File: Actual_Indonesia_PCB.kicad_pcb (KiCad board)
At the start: 2 copper layers, 157.7 x 133.2 mm, 88 parts, among them J1 USB_C_Receptacle_USB2.0_16P, J17 Screw_Terminal_01x02, J18 Screw_Terminal_01x02, J19 Screw_Terminal_01x02, J2 Conn_01x02_Pin, J20 Screw_Terminal_01x02, J21 Screw_Terminal_01x02, J22 Screw_Terminal_01x02, J23 Screw_Terminal_01x02, J24 Screw_Terminal_01x02, J25 Screw_Terminal_01x02, J26 Screw_Terminal_01x02, J27 Screw_Terminal_01x02, J28 Screw_Terminal_01x02, J29 Screw_Terminal_01x02, J30 Screw_Terminal_01x02, Q15 IRLZ44N, Q16 IRLZ44N, Q17 IRLZ44N, Q18 IRLZ44N, Q19 IRLZ44N, Q20 IRLZ44N, Q21 IRLZ44N, Q22 IRLZ44N, Q23 IRLZ44N, Q24 IRLZ44N, Q25 IRLZ44N, Q26 IRLZ44N, Q27 IRLZ44N, Q28 IRLZ44N, U1 ATmega328P-P, U4 LM7805_TO220, U5 CH340C, Y1 16MHz

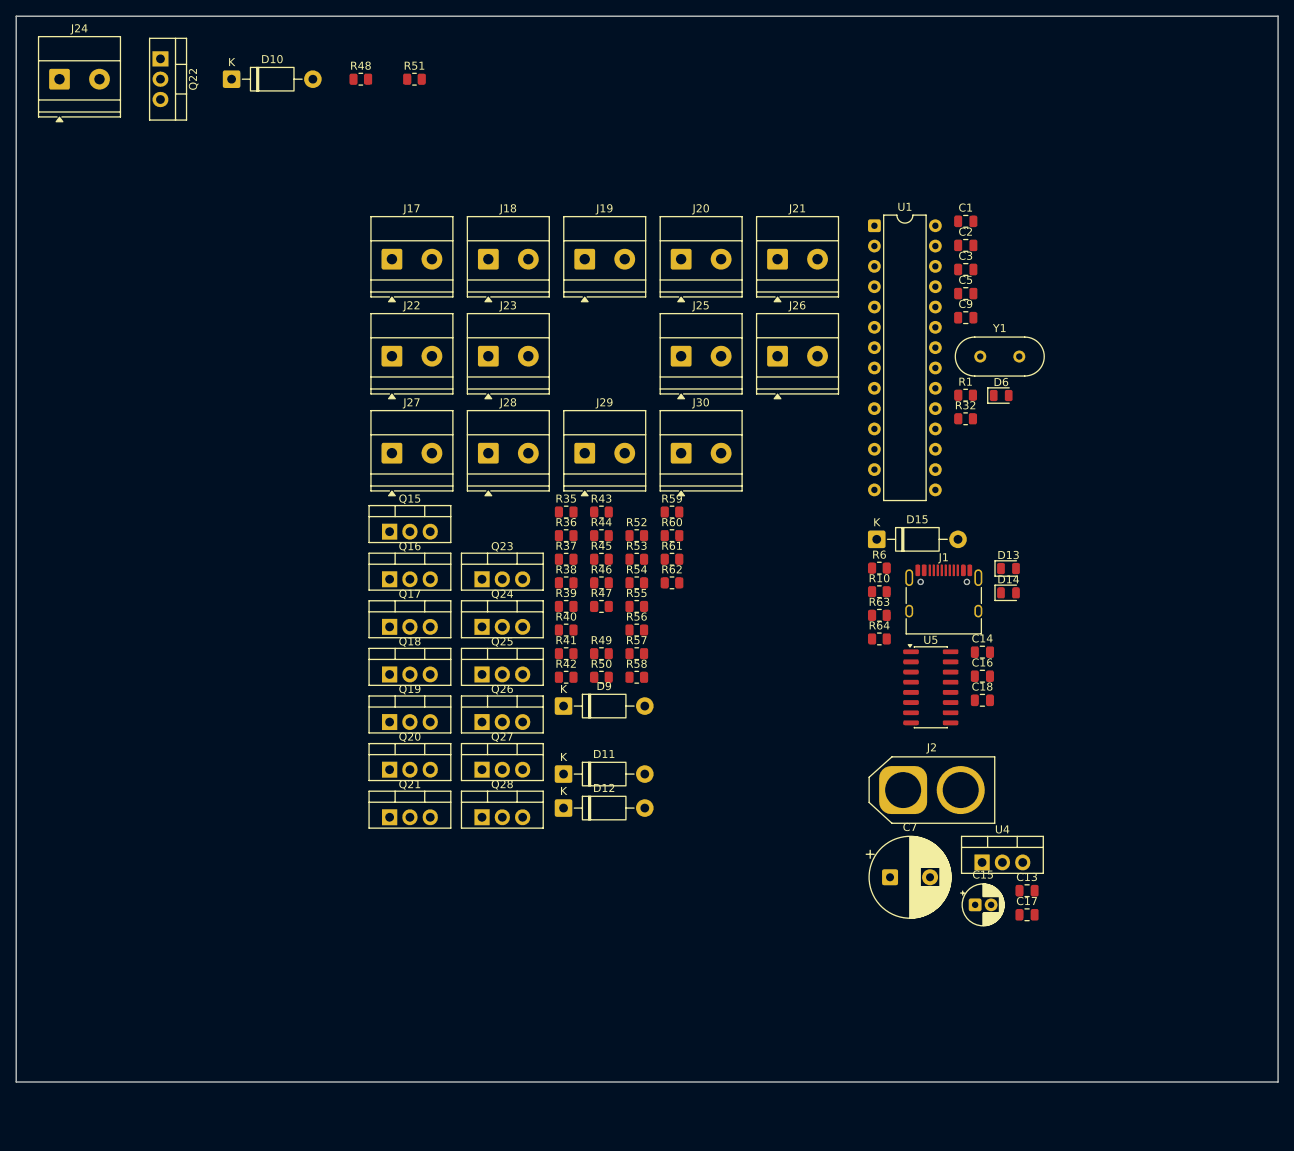
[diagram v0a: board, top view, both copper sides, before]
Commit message: Screw On Connectors Design
Started moving screw-on connectors to the edge similar to the example one.
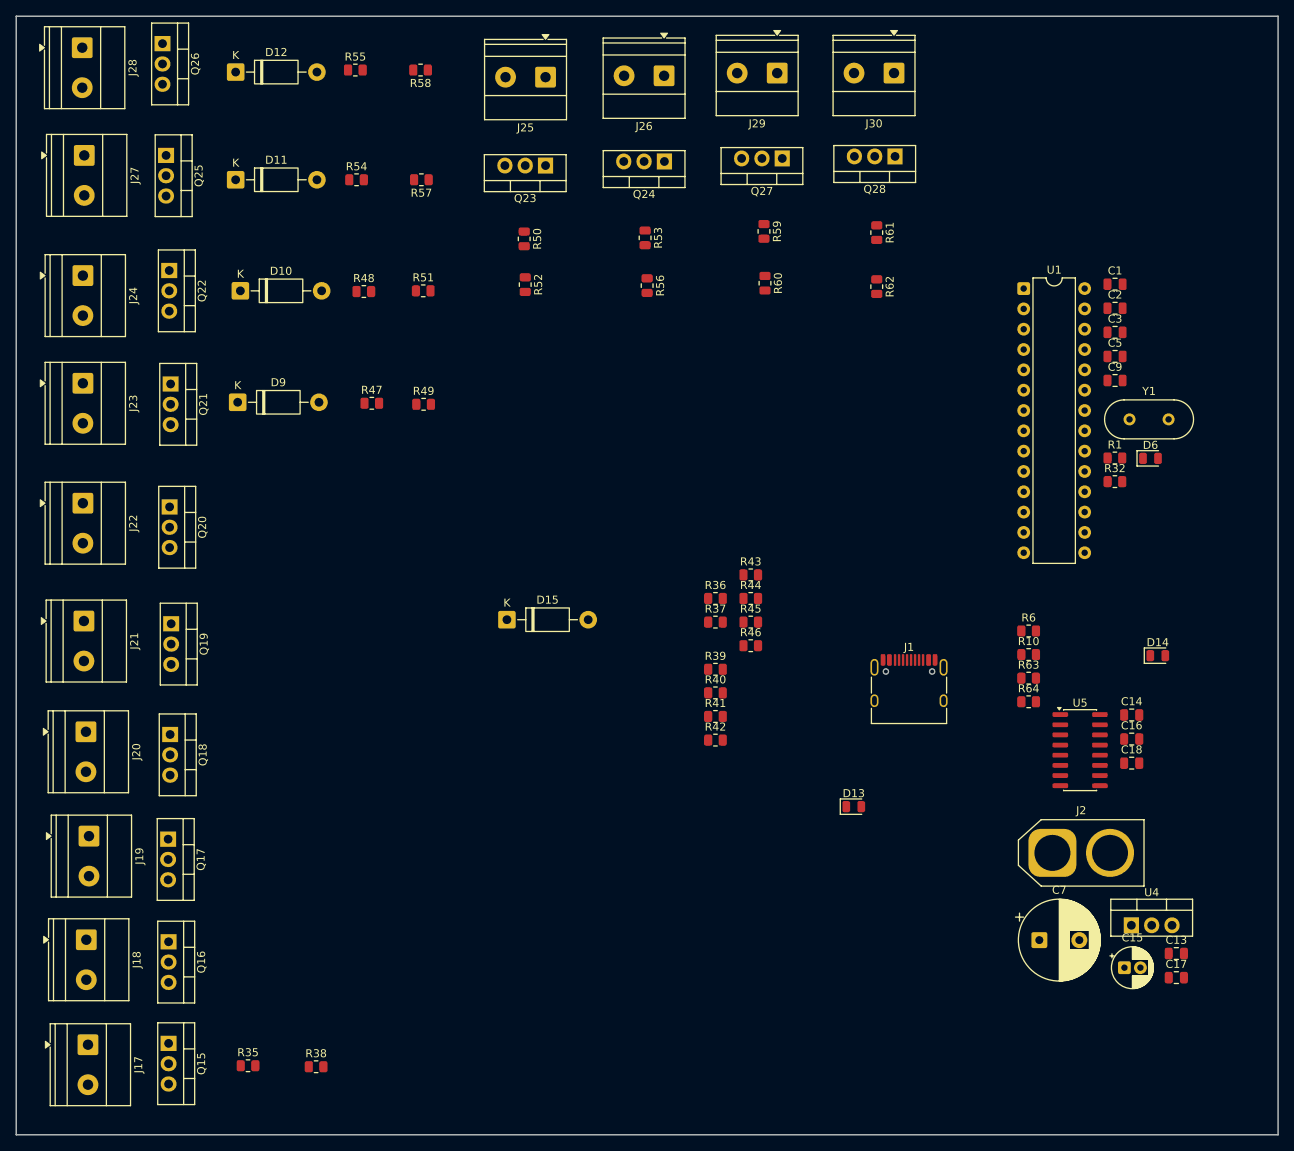
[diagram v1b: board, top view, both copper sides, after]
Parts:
- moved J17 105.3 mm to (74.8, 157.5), turned to -90 degrees
- moved D12 100.7 mm to (93.2, 35.9)
- moved J18 98.8 mm to (74.5, 144.4), turned to -90 degrees
- moved J21 97.8 mm to (74.2, 104.6), turned to -90 degrees
- moved Q28 97.4 mm to (175.6, 46.5), turned to 180 degrees
- moved J19 95.1 mm to (74.9, 131.4), turned to -90 degrees
- moved J20 95.0 mm to (74.5, 118.4), turned to -90 degrees
- moved Q26 93.7 mm to (84.1, 32.4), turned to -90 degrees
- moved Q27 85.1 mm to (161.5, 46.7), turned to 180 degrees
- moved D11 84.8 mm to (93.2, 49.4)
- moved R58 80.6 mm to (116.3, 35.7), turned to 180 degrees
- moved R35 79.8 mm to (94.8, 160.1)
- moved Q25 76.0 mm to (84.5, 46.4), turned to -90 degrees
- moved R55 75.7 mm to (108.2, 35.7)
- moved J28 71.7 mm to (74.0, 32.9), turned to -90 degrees
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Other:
- board size 157.7 x 133.2 mm -> 157.7 x 139.8 mm

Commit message: Switched the diodes on the fan to Schottkys and added a Schottky to input of power regulator
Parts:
- added D5: 1N5819, Diode_THT:D_DO-41_SOD81_P10.16mm_Horizontal, F.Cu at (176.6, 145.1)
- D10, D11, D12, D9: value 1N4007 -> 1N5819
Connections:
- C13 pad 2: +12V -> Net-(D5-K)
- J23 pad 2: Net-(D9-A) -> Net-(D11-A)
- J24 pad 2: Net-(D10-A) -> Net-(D9-A)
- J27 pad 2: Net-(D11-A) -> Net-(D10-A)
- Q21 pad 2: Net-(D9-A) -> Net-(D11-A)
- Q22 pad 2: Net-(D10-A) -> Net-(D9-A)
- Q25 pad 2: Net-(D11-A) -> Net-(D10-A)
- U4 pad 1: +12V -> Net-(D5-K)

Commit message: Fixed Schottky orientation, created 3 individual 12V pwr lines, fixed Schottky/resistor placement on layout
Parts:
- added C10: 470uF, Capacitor_THT:CP_Radial_D10.0mm_P5.00mm, F.Cu at (144.0, 152.7)
- added C8: 470uF, Capacitor_THT:CP_Radial_D10.0mm_P5.00mm, F.Cu at (144.0, 141.2)
- added J3: Conn_01x02_Pin, Connector_AMASS:AMASS_XT60-M_1x02_P7.20mm_Vertical, F.Cu at (157.5, 140.5)
- added J4: Conn_01x02_Pin, Connector_AMASS:AMASS_XT60-M_1x02_P7.20mm_Vertical, F.Cu at (157.5, 150.8)
- moved D11 36.5 mm to (82.5, 84.3), turned to 90 degrees
- moved D10 20.9 mm to (82.5, 45.7), turned to -90 degrees
- moved D9 20.1 mm to (82.5, 60.3), turned to -90 degrees
- moved R49 18.4 mm to (98.4, 75.6), turned to -90 degrees
- moved R51 18.3 mm to (98.4, 62.5), turned to -90 degrees
- moved R57 18.1 mm to (98.4, 47.2), turned to -90 degrees
- moved R58 18.1 mm to (98.4, 33.3), turned to -90 degrees
- moved R47 12.9 mm to (98.6, 82.8), turned to 90 degrees
- moved R48 12.5 mm to (98.4, 69.6), turned to 90 degrees
- moved D12 11.5 mm to (82.5, 31.8), turned to -90 degrees
- moved R54 11.1 mm to (98.4, 54.5), turned to 90 degrees
- moved R55 10.8 mm to (98.4, 40.4), turned to 90 degrees
- moved R62 8.71 mm to (169.7, 54.9), turned to 180 degrees
- moved R56 8.66 mm to (140.8, 54.9), turned to 180 degrees
- moved R60 8.44 mm to (155.4, 54.9), turned to 180 degrees
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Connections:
- C7 pad 1: +12V -> +12V_FANS
- D10 pad 1: +12V -> +12V_FANS
- D11 pad 1: +12V -> +12V_FANS
- D12 pad 1: +12V -> +12V_FANS
- D15 pad 1: Net-(D15-K) -> +5V
- D15 pad 2: +5V -> Net-(D15-A)
- D5 pad 2: +12V -> +12V_FANS
- D9 pad 1: +12V -> +12V_FANS
- J1 pad A4: Net-(D15-K) -> Net-(D15-A)
- J1 pad A9: Net-(D15-K) -> Net-(D15-A)
- J1 pad B4: Net-(D15-K) -> Net-(D15-A)
- J1 pad B9: Net-(D15-K) -> Net-(D15-A)
- J17 pad 1: +12V -> +12V_PADS
- J18 pad 1: +12V -> +12V_PADS
- J19 pad 1: +12V -> +12V_PADS
- J2 pad 1: +12V -> +12V_FANS
- J20 pad 1: +12V -> +12V_PADS
- J21 pad 1: +12V -> +12V_PADS
- J22 pad 1: +12V -> +12V_PADS
- J23 pad 1: +12V -> +12V_FANS
- J24 pad 1: +12V -> +12V_FANS
- J25 pad 1: +12V -> +12V_HEATERS
- J26 pad 1: +12V -> +12V_HEATERS
- J27 pad 1: +12V -> +12V_FANS
- J28 pad 1: +12V -> +12V_FANS
- J29 pad 1: +12V -> +12V_HEATERS
- J30 pad 1: +12V -> +12V_HEATERS

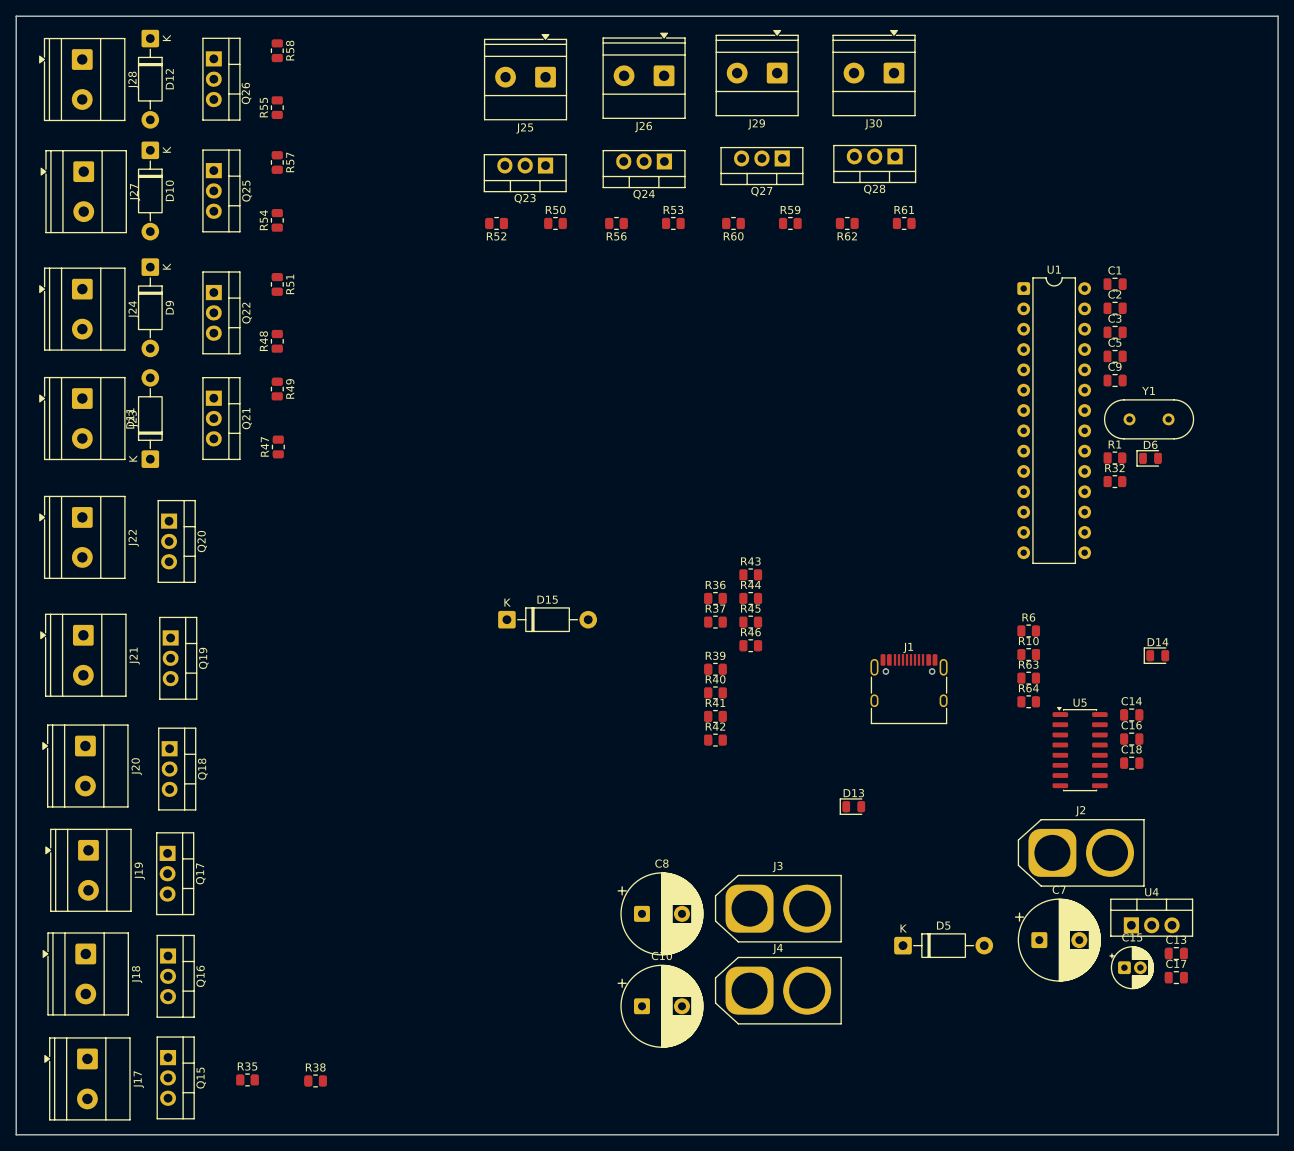
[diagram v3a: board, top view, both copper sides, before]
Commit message: Finished MOSFET/related component placement, placed power pins/capacitors
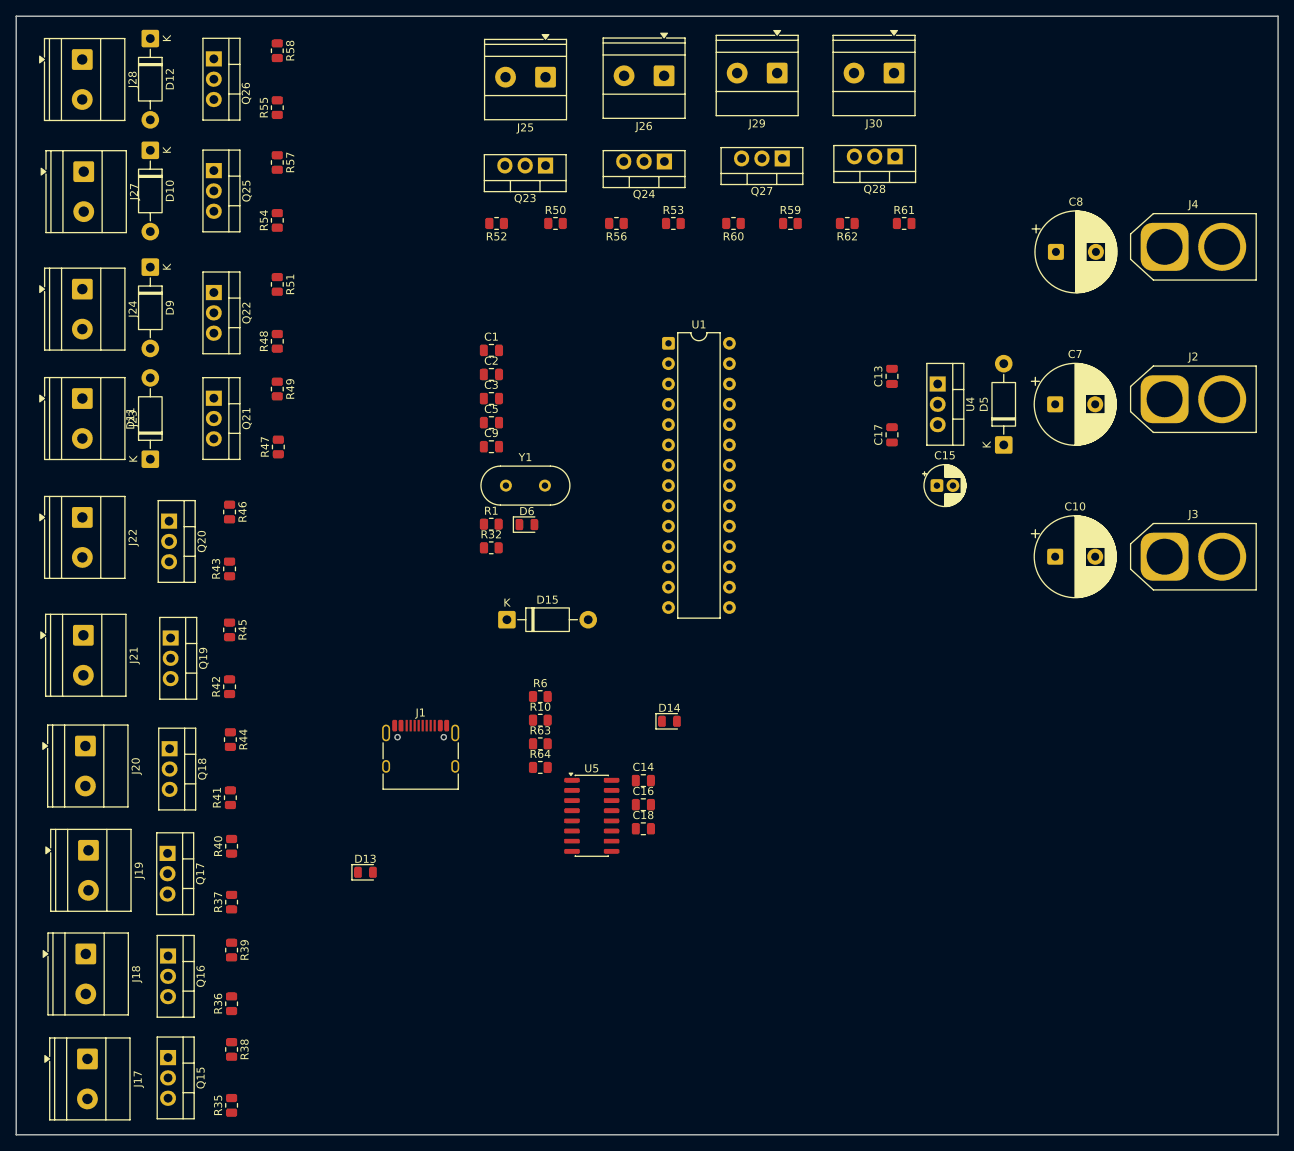
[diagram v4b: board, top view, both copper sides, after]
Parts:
- moved J4 106.5 mm to (209.3, 57.8)
- moved C8 97.6 mm to (195.8, 58.4)
- moved C13 80.4 mm to (175.3, 74.0), turned to 90 degrees
- moved R36 78.9 mm to (92.7, 152.4), turned to 90 degrees
- moved C1 78.4 mm to (125.2, 70.7)
- moved C2 78.4 mm to (125.2, 73.7)
- moved C3 78.4 mm to (125.2, 76.8)
- moved C5 78.4 mm to (125.2, 79.8)
- moved C9 78.4 mm to (125.2, 82.8)
- moved D6 78.4 mm to (129.6, 92.5)
- moved Y1 78.4 mm to (127.0, 87.6)
- moved R1 78.4 mm to (125.2, 92.5)
- moved R32 78.4 mm to (125.2, 95.4)
- moved C17 76.6 mm to (175.3, 81.3), turned to 90 degrees
- moved C10 76.3 mm to (195.7, 96.5)
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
